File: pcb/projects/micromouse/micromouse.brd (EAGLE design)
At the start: 80 x 100 mm, 52 parts, among them M1 332-06, M2 332-06, U1 DSPIC33FJ64MC804-H/PT, U2 UA78M33CKCS, U3 UA78M05CKCS

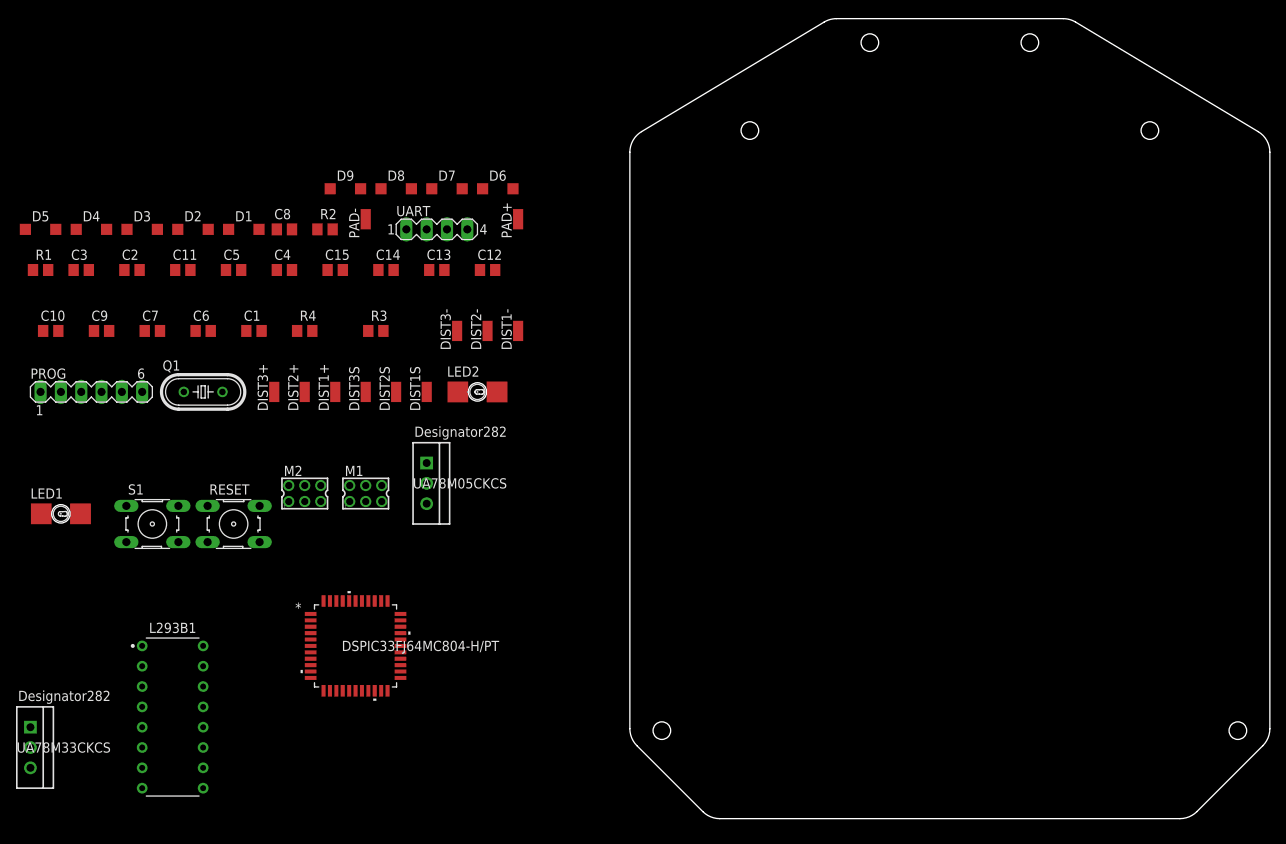
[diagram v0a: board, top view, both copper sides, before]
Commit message: Position components
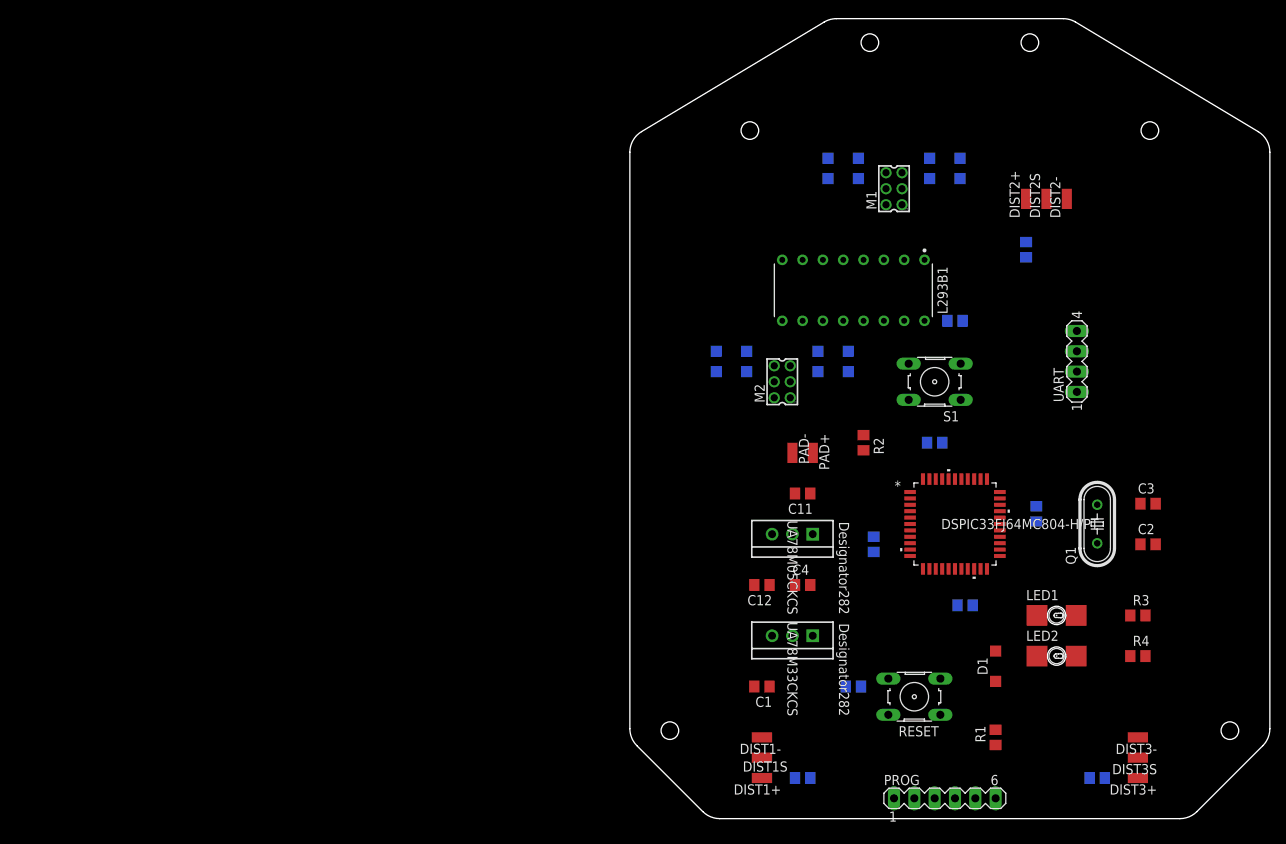
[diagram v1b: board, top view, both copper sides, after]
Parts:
- moved C10 142.2 mm to (58.4, 5.08), flipped to the bottom
- moved C3 136.5 mm to (64.8, 39.4)
- moved R1 132.9 mm to (45.7, 10.2), turned to 90 degrees
- moved C2 131.5 mm to (64.8, 34.3)
- moved LED1 125.1 mm to (53.3, 25.4)
- moved DIST3+ 118.2 mm to (63.5, 5.08), turned to 90 degrees
- moved PROG 118.2 mm to (39.4, 2.54)
- moved C9 116.0 mm to (49.5, 71.1), flipped to the bottom, turned to 270 degrees
- moved Q1 113.0 mm to (58.4, 36.8), turned to 90 degrees
- moved R4 111.8 mm to (63.5, 20.3)
- moved D1 108.7 mm to (45.7, 19.1), turned to 90 degrees
- moved D4 106.9 mm to (39.4, 80.0), flipped to the bottom
- moved DIST3S 106.8 mm to (63.5, 7.62), turned to 90 degrees
- moved R3 101.7 mm to (63.5, 25.4)
- moved D5 100.5 mm to (26.7, 80.0), flipped to the bottom, turned to 180 degrees
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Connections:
- net M1_EA: now also M1.2, U1.4; no longer M1.1, U1.3
- net M1_EB: now also M1.1, U1.3; no longer M1.2, U1.4
- net M2_EA: now also M2.2, U1.35; no longer M2.1, U1.36
- net M2_EB: now also M2.1, U1.36; no longer M2.2, U1.35
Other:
- board text added: "Back"
- board text added: "Dashed area should not be used to place components because parts will be mounted there."
- board text added: "Front"
- board text added: "Motor"
- board text added: "Sensor"

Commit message: Most wiring done
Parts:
- moved S1 40.9 mm to (62.2, 21.6)
- moved R2 35.9 mm to (54.6, 21.6), turned to 90 degrees
- moved LED1 29.5 mm to (57.1, 54.6)
- moved LED2 29.5 mm to (57.1, 49.5)
- moved R3 29.2 mm to (64.8, 54.6)
- moved R4 29.2 mm to (64.8, 49.5)
- moved D1 15.3 mm to (30.5, 17.8)
- moved R1 15.2 mm to (30.5, 10.2)
- moved UART 8.03 mm to (58.4, 64.8), turned to 0 degrees
- moved C2 5.08 mm to (64.8, 39.4)
- moved C3 5.08 mm to (64.8, 34.3)
- moved C15 4.58 mm to (38.1, 24.1), turned to 0 degrees
- moved D8 4.02 mm to (24.1, 52.1), turned to 90 degrees
- moved RESET 4.02 mm to (39.4, 16.5)
- moved C9 3.81 mm to (45.7, 71.1), turned to 0 degrees
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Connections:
- net BUTTON: now also U1.26; no longer U1.34
- net DSENS2: now also U1.25; no longer U1.24
- net DSENS3: now also U1.24; no longer U1.25
- net M1_D1: now also U1.38; no longer U1.1
- net M1_D2: now also U1.37; no longer U1.2
- net M1_EA: now also U1.35; no longer U1.4
- net M1_EB: now also U1.36; no longer U1.3
- net M2_D1: now also U1.2; no longer U1.38
- net M2_D2: now also U1.1; no longer U1.37
- net M2_EA: now also U1.4; no longer U1.35
- net M2_EB: now also U1.3; no longer U1.36
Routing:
- net VDD: track 0.00 -> 206.4 mm, vias 0 -> 4
- net +5V: track 0.00 -> 181.0 mm, vias 0 -> 5
- net PAD+: track 0.00 -> 68.8 mm, vias 0 -> 2
- net DSENS2: track 0.00 -> 68.7 mm, vias 0 -> 2
- net DSENS1: track 0.00 -> 56.7 mm, vias 0 -> 2
- net DSENS3: track 0.00 -> 39.2 mm
- net TX: track 0.00 -> 39.0 mm
- net M2_PWM: track 0.00 -> 36.8 mm, vias 0 -> 2
- net RX: track 0.00 -> 36.6 mm
- net M2_D1: track 0.00 -> 29.3 mm
- net N$8: track 0.00 -> 29.2 mm
- net N$9: track 0.00 -> 28.9 mm
- net M2_EA: track 0.00 -> 26.6 mm
- net M1-: track 0.00 -> 26.0 mm
- net M2_D2: track 0.00 -> 25.1 mm
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
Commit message: Complete wiring
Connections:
- net M1_D1: now also U1.37; no longer U1.38
- net M1_D2: now also U1.38; no longer U1.37
- net M1_EA: now also U1.36; no longer U1.35
- net M1_EB: now also U1.35; no longer U1.36
- net M1_PWM: now also U1.10; no longer U1.14
- net M2_PWM: now also U1.14; no longer U1.10
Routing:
- net M1_D2: track 0.00 -> 47.4 mm, vias 0 -> 2
- net M1_EA: track 0.00 -> 47.1 mm, vias 0 -> 2
- net M1_EB: track 0.00 -> 46.8 mm, vias 0 -> 2
- net M1_PWM: track 0.00 -> 41.2 mm, vias 0 -> 1
- net VDD: track 206.4 -> 244.1 mm, vias 4 -> 5
- net M1_D1: track 0.00 -> 35.8 mm, vias 0 -> 2
- net PAD+: track 68.8 -> 100.3 mm
- net M2_PWM: track 36.8 -> 47.0 mm
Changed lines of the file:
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@@
 <wire x1="27.94" y1="20.32" x2="29.845" y2="22.225" width="0.508" layer="1"/>
 <wire x1="29.845" y1="22.225" x2="31.115" y2="23.495" width="0.508" layer="1"/>
-<wire x1="31.115" y1="23.495" x2="36.83" y2="29.21" width="0.508" layer="1"/>
-<wire x1="36.83" y1="29.21" x2="40.64" y2="29.21" width="0.508" layer="1"/>
 <wire x1="40.64" y1="29.21" x2="45.72" y2="29.21" width="0.508" layer="16"/>
 <wire x1="45.72" y1="29.21" x2="48.26" y2="31.75" width="0.508" layer="16"/>
@@
 <wire x1="25.4" y1="40.64" x2="15.24" y2="50.8" width="0.508" layer="16"/>
 <wire x1="15.24" y1="50.8" x2="15.24" y2="53.34" width="0.508" layer="16"/>
-<wire x1="36.83" y1="62.23" x2="32.02" y2="78.74" width="0" layer="19" extent="1-1"/>
+<wire x1="31.115" y1="23.495" x2="34.29" y2="26.67" width="0.508" layer="1"/>
+<wire x1="34.29" y1="26.67" x2="38.1" y2="26.67" width="0.508" layer="1"/>
+<wire x1="38.1" y1="26.67" x2="40.64" y2="29.21" width="0.508" layer="1"/>
+<wire x1="18.05" y1="54.61" x2="16.51" y2="54.61" width="0.508" layer="1"/>
+<wire x1="16.51" y1="54.61" x2="15.24" y2="55.88" width="0.508" layer="1"/>
+<wire x1="15.24" y1="55.88" x2="15.24" y2="66.04" width="0.508" layer="1"/>
+<wire x1="15.24" y1="66.04" x2="16.51" y2="67.31" width="0.508" layer="1"/>
+<wire x1="16.51" y1="67.31" x2="19.05" y2="67.31" width="0.508" layer="1"/>
+<wire x1="19.05" y1="67.31" x2="20.32" y2="68.58" width="0.508" layer="1"/>
+<wire x1="20.32" y1="68.58" x2="20.32" y2="72.39" width="0.508" layer="1"/>
+<wire x1="20.32" y1="72.39" x2="22.86" y2="74.93" width="0.508" layer="1"/>
+<via x="22.86" y="74.93" extent="1-16" drill="0.35" diameter="0.55"/>
+<wire x1="22.86" y1="74.93" x2="24.13" y2="76.2" width="0.508" layer="16"/>
+<wire x1="29.48" y1="76.2" x2="32.02" y2="78.74" width="0.508" layer="16"/>
+<wire x1="24.13" y1="76.2" x2="29.48" y2="76.2" width="0.508" layer="16"/>
 <wire x1="46.2534" y1="36.83" x2="39.84" y2="42.4434" width="0" layer="19" extent="1-1"/>
 </signal>
@@
 <wire x1="24.13" y1="50.17" x2="24.13" y2="48.26" width="0.508" layer="16"/>
 <via x="24.13" y="48.26" extent="1-16" drill="0.35"/>
-<wire x1="24.77" y1="80.01" x2="41.27" y2="80.01" width="0" layer="19" extent="16-16"/>
+<wire x1="41.27" y1="80.01" x2="43.18" y2="81.92" width="0.508" layer="16"/>
+<wire x1="43.18" y1="81.92" x2="43.18" y2="85.09" width="0.508" layer="16"/>
+<wire x1="43.18" y1="85.09" x2="41.91" y2="86.36" width="0.508" layer="16"/>
+<wire x1="25.4" y1="86.36" x2="22.86" y2="83.82" width="0.508" layer="16"/>
+<wire x1="22.86" y1="83.82" x2="22.86" y2="80.01" width="0.508" layer="16"/>
+<wire x1="41.91" y1="86.36" x2="25.4" y2="86.36" width="0.508" layer="16"/>
 </signal>
 <signal name="GND">
@@
 <signal name="M1_EB">
 <contactref element="M1" pad="1"/>
-<contactref element="U1" pad="36"/>
-<wire x1="43.04" y1="42.4434" x2="34.02" y2="76.74" width="0" layer="19" extent="1-1"/>
+<contactref element="U1" pad="35"/>
+<wire x1="43.84" y1="42.4434" x2="43.84" y2="45.695" width="0.508" layer="1"/>
+<wire x1="43.84" y1="45.695" x2="43.815" y2="45.72" width="0.508" layer="1"/>
+<via x="43.815" y="45.72" extent="1-16" drill="0.35" diameter="0.55"/>
+<wire x1="43.815" y1="45.72" x2="43.815" y2="50.165" width="0.508" layer="16"/>
+<wire x1="43.815" y1="50.165" x2="46.99" y2="53.34" width="0.508" layer="16"/>
+<wire x1="46.99" y1="53.34" x2="46.99" y2="55.88" width="0.508" layer="16"/>
+<via x="46.99" y="55.88" extent="1-16" drill="0.35" diameter="0.55"/>
+<wire x1="46.99" y1="55.88" x2="46.99" y2="73.66" width="0.508" layer="1"/>
+<wire x1="43.91" y1="76.74" x2="34.02" y2="76.74" width="0.508" layer="1"/>
+<wire x1="46.99" y1="73.66" x2="43.91" y2="76.74" width="0.508" layer="1"/>
 </signal>
 <signal name="M1_EA">
 <contactref element="M1" pad="2"/>
-<contactref element="U1" pad="35"/>
-<wire x1="43.84" y1="42.4434" x2="32.02" y2="76.74" width="0" layer="19" extent="1-1"/>
+<contactref element="U1" pad="36"/>
+<wire x1="32.02" y1="76.74" x2="32.02" y2="74.66" width="0.508" layer="1"/>
+<wire x1="32.02" y1="74.66" x2="33.02" y2="73.66" width="0.508" layer="1"/>
+<wire x1="33.02" y1="73.66" x2="43.18" y2="73.66" width="0.508" layer="1"/>
+<wire x1="43.18" y1="73.66" x2="45.72" y2="71.12" width="0.508" layer="1"/>
+<wire x1="45.72" y1="71.12" x2="45.72" y2="55.88" width="0.508" layer="1"/>
+<via x="45.72" y="55.88" extent="1-16" drill="0.35" diameter="0.55"/>
+<wire x1="45.72" y1="53.34" x2="45.72" y2="55.88" width="0.508" layer="16"/>
+<wire x1="43.04" y1="42.4434" x2="43.04" y2="45.606" width="0.508" layer="1"/>
+<wire x1="43.04" y1="45.606" x2="42.926" y2="45.72" width="0.508" layer="1"/>
+<via x="42.926" y="45.72" extent="1-16" drill="0.35" diameter="0.55"/>
+<wire x1="42.926" y1="45.72" x2="43.0304" y2="45.8244" width="0.508" layer="16"/>
+<wire x1="43.0304" y1="45.8244" x2="43.0304" y2="50.6504" width="0.508" layer="16"/>
+<wire x1="43.0304" y1="50.6504" x2="45.72" y2="53.34" width="0.508" layer="16"/>
 </signal>
 <signal name="M1-">
@@
 <signal name="M1_D1">
 <contactref element="L293B1" pad="INPUT1"/>
-<contactref element="U1" pad="38"/>
-<wire x1="41.44" y1="42.4434" x2="34.29" y2="69.85" width="0" layer="19" extent="1-1"/>
+<contactref element="U1" pad="37"/>
+<wire x1="42.24" y1="42.4434" x2="42.24" y2="46.66" width="0.508" layer="1"/>
+<wire x1="42.24" y1="46.66" x2="41.91" y2="46.99" width="0.508" layer="1"/>
+<via x="41.91" y="46.99" extent="1-16" drill="0.35" diameter="0.55"/>
+<wire x1="41.91" y1="46.99" x2="41.91" y2="50.8" width="0.508" layer="16"/>
+<via x="41.91" y="50.8" extent="1-16" drill="0.35" diameter="0.55"/>
+<wire x1="41.91" y1="50.8" x2="44.45" y2="53.34" width="0.508" layer="1"/>
+<wire x1="44.45" y1="53.34" x2="44.45" y2="63.5" width="0.508" layer="1"/>
+<wire x1="40.64" y1="67.31" x2="35.56" y2="67.31" width="0.508" layer="1"/>
+<wire x1="35.56" y1="67.31" x2="34.29" y2="68.58" width="0.508" layer="1"/>
+<wire x1="34.29" y1="68.58" x2="34.29" y2="69.85" width="0.508" layer="1"/>
+<wire x1="44.45" y1="63.5" x2="40.64" y2="67.31" width="0.508" layer="1"/>
 </signal>
 <signal name="M1_D2">
 <contactref element="L293B1" pad="INPUT2"/>
-<contactref element="U1" pad="37"/>
-<wire x1="42.24" y1="42.4434" x2="21.59" y2="69.85" width="0" layer="19" extent="1-1"/>
+<contactref element="U1" pad="38"/>
+<wire x1="41.44" y1="42.4434" x2="41.44" y2="46.19" width="0.508" layer="1"/>
+<wire x1="41.44" y1="46.19" x2="40.64" y2="46.99" width="0.508" layer="1"/>
+<via x="40.64" y="46.99" extent="1-16" drill="0.35" diameter="0.55"/>
+<wire x1="40.64" y1="46.99" x2="40.64" y2="50.8" width="0.508" layer="16"/>
+<via x="40.64" y="50.8" extent="1-16" drill="0.35" diameter="0.55"/>
+<wire x1="40.64" y1="50.8" x2="43.18" y2="53.34" width="0.508" layer="1"/>
+<wire x1="43.18" y1="53.34" x2="43.18" y2="62.23" width="0.508" layer="1"/>
+<wire x1="43.18" y1="62.23" x2="39.37" y2="66.04" width="0.508" layer="1"/>
+<wire x1="22.86" y1="66.04" x2="21.59" y2="67.31" width="0.508" layer="1"/>
+<wire x1="21.59" y1="67.31" x2="21.59" y2="69.85" width="0.508" layer="1"/>
+<wire x1="39.37" y1="66.04" x2="22.86" y2="66.04" width="0.508" layer="1"/>
 </signal>
 <signal name="M1_PWM">
 <contactref element="L293B1" pad="ENABLE1"/>
-<contactref element="U1" pad="14"/>
-<wire x1="38.24" y1="31.2166" x2="36.83" y2="69.85" width="0" layer="19" extent="1-1"/>
+<contactref element="U1" pad="10"/>
+<wire x1="35.0266" y1="33.63" x2="32.41" y2="33.63" width="0.508" layer="1"/>
+<wire x1="32.41" y1="33.63" x2="31.75" y2="34.29" width="0.508" layer="1"/>
+<wire x1="31.75" y1="34.29" x2="31.75" y2="37.6454" width="0.508" layer="1"/>
+<via x="31.75" y="37.6454" extent="1-16" drill="0.35" diameter="0.55"/>
+<wire x1="31.75" y1="37.6454" x2="31.75" y2="45.72" width="0.508" layer="16"/>
+<wire x1="31.75" y1="45.72" x2="33.02" y2="46.99" width="0.508" layer="16"/>
+<wire x1="33.02" y1="46.99" x2="33.02" y2="66.04" width="0.508" layer="16"/>
+<wire x1="33.02" y1="66.04" x2="36.83" y2="69.85" width="0.508" layer="16"/>
 </signal>
 <signal name="M2_EB">
@@
 <signal name="M2_PWM">
 <contactref element="L293B1" pad="ENABLE2"/>
-<contactref element="U1" pad="10"/>
 <wire x1="19.05" y1="62.23" x2="19.05" y2="59.69" width="0.508" layer="1"/>
 <wire x1="19.05" y1="59.69" x2="26.67" y2="52.07" width="0.508" layer="1"/>
@@
 <wire x1="30.48" y1="48.26" x2="30.48" y2="38.1" width="0.508" layer="16"/>
 <via x="30.48" y="38.1" extent="1-16" drill="0.35"/>
-<wire x1="30.48" y1="35.56" x2="30.48" y2="38.1" width="0.508" layer="1"/>
-<wire x1="35.0266" y1="33.63" x2="32.41" y2="33.63" width="0.508" layer="1"/>
-<wire x1="32.41" y1="33.63" x2="30.48" y2="35.56" width="0.508" layer="1"/>
+<contactref element="U1" pad="14"/>
+<wire x1="38.24" y1="31.2166" x2="38.24" y2="29.35" width="0.508" layer="1"/>
+<wire x1="38.24" y1="29.35" x2="36.83" y2="27.94" width="0.508" layer="1"/>
+<wire x1="36.83" y1="27.94" x2="34.29" y2="27.94" width="0.508" layer="1"/>
+<wire x1="34.29" y1="27.94" x2="30.48" y2="31.75" width="0.508" layer="1"/>
+<wire x1="30.48" y1="31.75" x2="30.48" y2="38.1" width="0.508" layer="1"/>
 </signal>
 <signal name="M2_D1">

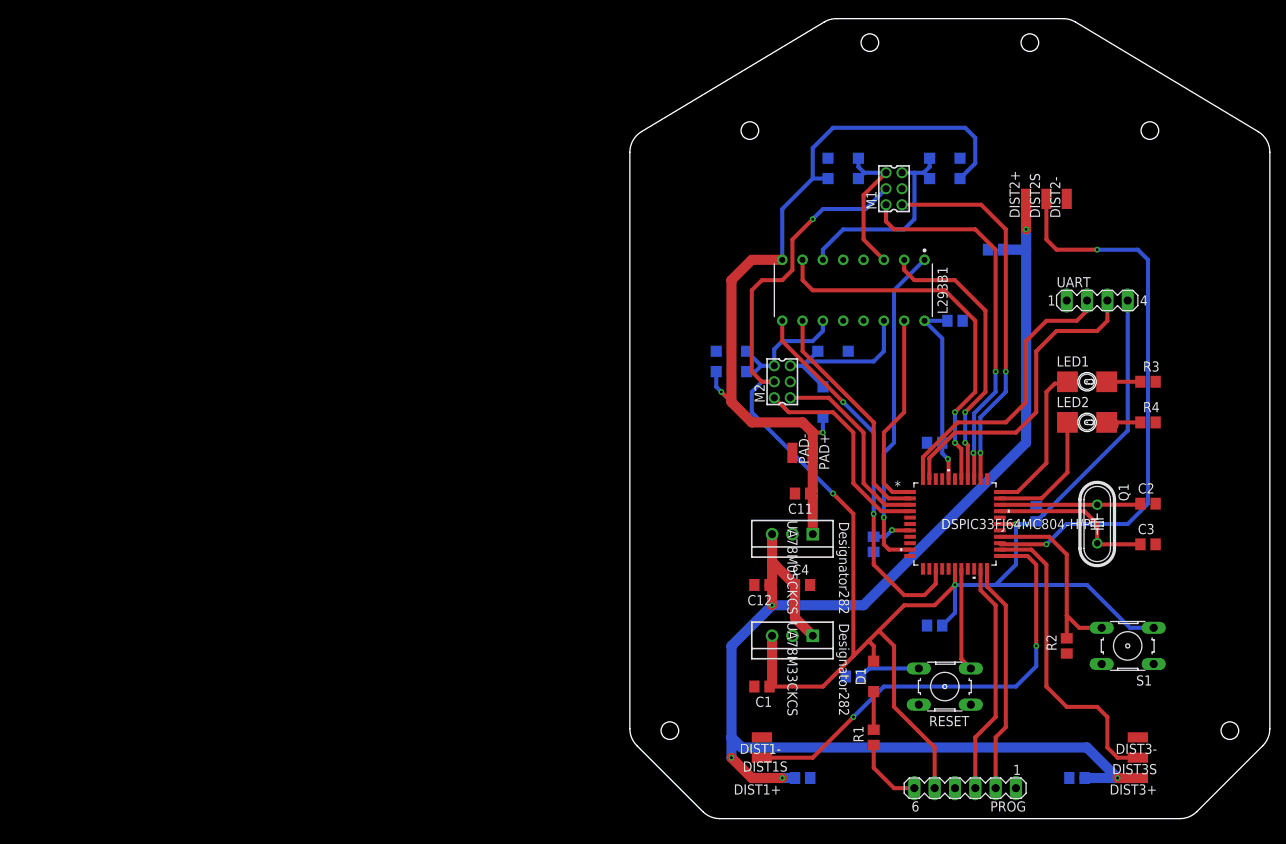
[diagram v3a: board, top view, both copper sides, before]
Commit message: Ground plane and ground connections
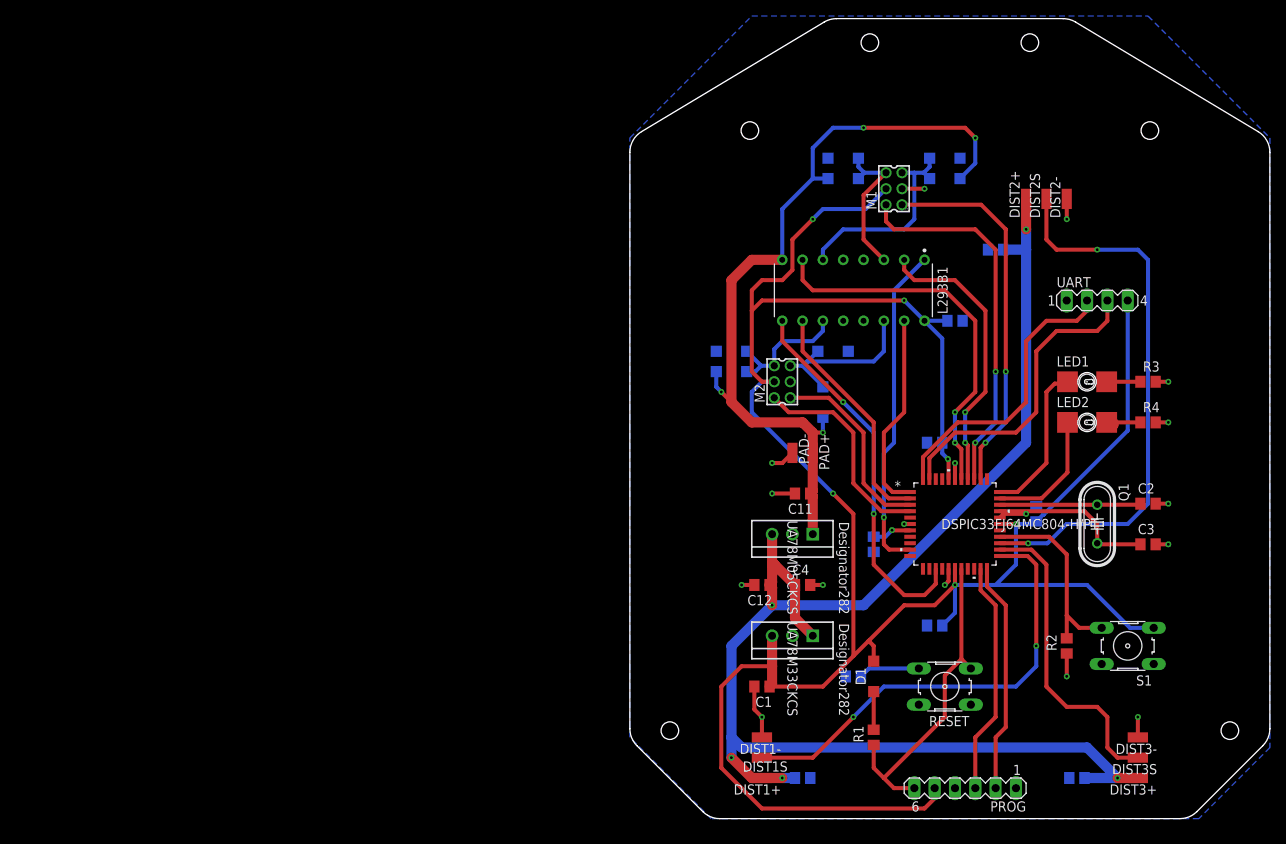
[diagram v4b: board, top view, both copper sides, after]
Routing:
- net VDD: track 244.1 -> 292.9 mm, vias 5 -> 6
- net GND: track 0.00 -> 41.4 mm, vias 0 -> 17
- net N$6: track 21.9 -> 40.8 mm
- net N$13: track 5.07 -> 6.54 mm
- net DSENS2: track 68.7 -> 69.9 mm
- net PAD+: vias 2 -> 4
- added copper zone on layer 16, net GND
